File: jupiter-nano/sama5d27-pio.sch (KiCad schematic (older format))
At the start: 3 parts

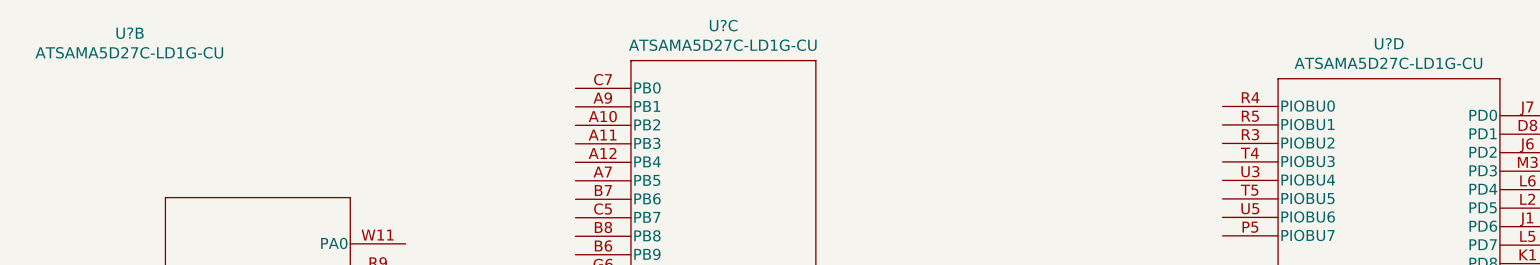
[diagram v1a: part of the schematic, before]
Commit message: WIP some work on clocking
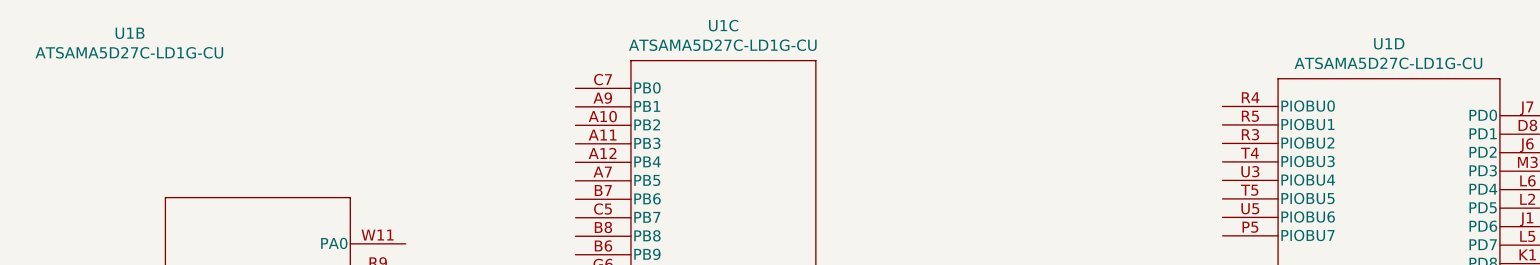
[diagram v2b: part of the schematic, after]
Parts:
- gave numbers to parts that had none: 1
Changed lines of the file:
@@
 $EndDescr
 $Comp
-L ATSAMA5D27C-LD1G:ATSAMA5D27C-LD1G-CU U?
+L ATSAMA5D27C-LD1G:ATSAMA5D27C-LD1G-CU U1
 U 2 1 5F5990A8
 P 2382 1089
-F 0 "U?" H 1740 1576 60  0000 C CNN
+F 0 "U1" H 1740 1576 60  0000 C CNN
 F 1 "ATSAMA5D27C-LD1G-CU" H 1740 1470 60  0000 C CNN
 F 2 "TFBGA361_16X16_MCH" H 3582 1429 60  0001 C CNN
@@
 $EndComp
 $Comp
-L ATSAMA5D27C-LD1G:ATSAMA5D27C-LD1G-CU U?
+L ATSAMA5D27C-LD1G:ATSAMA5D27C-LD1G-CU U1
 U 3 1 5F5A7AFC
 P 4150 948
-F 0 "U?" H 4950 1335 60  0000 C CNN
+F 0 "U1" H 4950 1335 60  0000 C CNN
 F 1 "ATSAMA5D27C-LD1G-CU" H 4950 1229 60  0000 C CNN
 F 2 "TFBGA361_16X16_MCH" H 5350 1288 60  0001 C CNN
@@
 $EndComp
 $Comp
-L ATSAMA5D27C-LD1G:ATSAMA5D27C-LD1G-CU U?
+L ATSAMA5D27C-LD1G:ATSAMA5D27C-LD1G-CU U1
 U 4 1 5F5C0676
 P 7650 1046
-F 0 "U?" H 8550 1433 60  0000 C CNN
+F 0 "U1" H 8550 1433 60  0000 C CNN
 F 1 "ATSAMA5D27C-LD1G-CU" H 8550 1327 60  0000 C CNN
 F 2 "TFBGA361_16X16_MCH" H 8850 1386 60  0001 C CNN

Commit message: WIP, PIO done
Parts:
- added R14: 100K, symbol Device:R_Small
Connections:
- net labels added: AD0, AD1, AD2, AD3, AD4, AD5, ADTRG-IRQ, FLEXCOM4_IO1, GND, I2C_TWCK0, I2C_TWCK1, I2C_TWD0, I2C_TWD1, LOWQ#, PIOBU1, PIOBU2, PIOBU3, PIOBU4, PIOBU5, PIOBU6, PIOBU7, PMIC_CHLEV_PA12, PMIC_IRQ_B13, PMIC_LBO, PWMEXTRAG1-IRQ, PWMH1, PWMH2, PWMH3, PWML0, SDMMC_CD, SDMMC_CK, SDMMC_CMD, SDMMC_DAT0, SDMMC_DAT1, SDMMC_DAT2, SDMMC_DAT3, SPI_MISO, SPI_MOSI, STATUS_LED, TMS, UART1_RX, UART1_TX
- wire segments 0 -> 47
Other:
- moved on the sheet: U1B, U1C, U1D
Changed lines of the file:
@@
 L ATSAMA5D27C-LD1G:ATSAMA5D27C-LD1G-CU U1
 U 2 1 5F5990A8
-P 2382 1089
-F 0 "U1" H 1740 1576 60  0000 C CNN
-F 1 "ATSAMA5D27C-LD1G-CU" H 1740 1470 60  0000 C CNN
-F 2 "TFBGA361_16X16_MCH" H 3582 1429 60  0001 C CNN
-F 3 "" H 2382 1089 60  0000 C CNN
-	2    2382 1089
-	1    0    0    -1
-$EndComp
+P 1150 600
+F 0 "U1" H 1195 400 60  0000 C CNN
+F 1 "ATSAMA5D27C-LD1G-CU" H 1195 300 60  0000 C CNN
+F 2 "TFBGA361_16X16_MCH" H 2350 940 60  0001 C CNN
+F 3 "" H 1150 600 60  0000 C CNN
+	2    1150 600
+	1    0    0    -1
+$EndComp
+$Comp
+L ATSAMA5D27C-LD1G:ATSAMA5D27C-LD1G-CU U1
+U 4 1 5F5C0676
+P 7250 1400
+F 0 "U1" H 8150 1787 60  0000 C CNN
+F 1 "ATSAMA5D27C-LD1G-CU" H 8150 1681 60  0000 C CNN
+F 2 "TFBGA361_16X16_MCH" H 8450 1740 60  0001 C CNN
+F 3 "" H 7250 1400 60  0000 C CNN
+	4    7250 1400
+	1    0    0    -1
+$EndComp
+Wire Wire Line
+	2000 2150 2250 2150
+Text GLabel 2250 2150 2    50   Input ~ 0
+STATUS_LED
+Text GLabel 2250 3050 2    50   Input ~ 0
+PMIC_CHLEV_PA12
+Text GLabel 2250 3500 2    50   Input ~ 0
+SPI_MOSI
+Text GLabel 2250 3650 2    50   Input ~ 0
+SPI_MISO
+Text GLabel 2250 3950 2    50   Input ~ 0
+SDMMC_DAT0
+Text GLabel 2200 4100 2    50   Input ~ 0
+SDMMC_DAT1
+Text GLabel 2200 4250 2    50   Input ~ 0
+SDMMC_DAT2
+Text GLabel 2250 4400 2    50   Input ~ 0
+SDMMC_DAT3
+Text GLabel 2250 4550 2    50   Input ~ 0
+SDMMC_CK
+Text GLabel 2250 5450 2    50   Input ~ 0
+SDMMC_CMD
+Text GLabel 2250 5750 2    50   Input ~ 0
+SDMMC_CD
+Text GLabel 2250 5900 2    50   Input ~ 0
+PWML0
+Text GLabel 3900 1500 0    50   Input ~ 0
+PWML0
+Wire Wire Line
+	2000 3050 2250 3050
+Wire Wire Line
+	2000 3500 2250 3500
+Wire Wire Line
+	2000 3650 2250 3650
 $Comp
 L ATSAMA5D27C-LD1G:ATSAMA5D27C-LD1G-CU U1
 U 3 1 5F5A7AFC
-P 4150 948
-F 0 "U1" H 4950 1335 60  0000 C CNN
-F 1 "ATSAMA5D27C-LD1G-CU" H 4950 1229 60  0000 C CNN
-F 2 "TFBGA361_16X16_MCH" H 5350 1288 60  0001 C CNN
-F 3 "" H 4150 948 60  0000 C CNN
-	3    4150 948
-	1    0    0    -1
-$EndComp
-$Comp
-L ATSAMA5D27C-LD1G:ATSAMA5D27C-LD1G-CU U1
-U 4 1 5F5C0676
-P 7650 1046
-F 0 "U1" H 8550 1433 60  0000 C CNN
-F 1 "ATSAMA5D27C-LD1G-CU" H 8550 1327 60  0000 C CNN
-F 2 "TFBGA361_16X16_MCH" H 8850 1386 60  0001 C CNN
-F 3 "" H 7650 1046 60  0000 C CNN
-	4    7650 1046
-	1    0    0    -1
+P 4150 1450
+F 0 "U1" H 4950 1837 60  0000 C CNN
+F 1 "ATSAMA5D27C-LD1G-CU" H 4950 1731 60  0000 C CNN
+F 2 "TFBGA361_16X16_MCH" H 5350 1790 60  0001 C CNN
+F 3 "" H 4150 1450 60  0000 C CNN
+	3    4150 1450
+	1    0    0    -1
+$EndComp
+Wire Wire Line
+	2000 1250 2100 1250
+Wire Wire Line
+	2000 1400 2100 1400
+Wire Wire Line
+	4150 1400 3900 1400
+Wire Wire Line
+	3900 1500 4150 1500
+Wire Wire Line
+	2000 3950 2250 3950
+Wire Wire Line
+	2000 4100 2200 4100
+Wire Wire Line
+	2000 4250 2200 4250
+Wire Wire Line
+	2000 4400 2250 4400
+Wire Wire Line
+	2000 4550 2250 4550
+Wire Wire Line
+	2000 5450 2250 5450
+Wire Wire Line
+	2000 5750 2250 5750
+Wire Wire Line
+	2000 5900 2250 5900
+Text GLabel 3900 1400 0    50   Input ~ 0
+PWMH1
+Text GLabel 3900 1700 0    50   Input ~ 0
+PWMEXTRAG1-IRQ
+Text GLabel 3900 1900 0    50   Input ~ 0
+PWMH2
+Text GLabel 3900 2100 0    50   Input ~ 0
+PWMH3
+Wire Wire Line
+	3900 1700 4150 1700
+Wire Wire Line
+	3900 1900 4150 1900
+Wire Wire Line
+	3900 2100 4150 2100
+Text GLabel 3900 2700 0    50   Input ~ 0
+PMIC_IRQ_B13
+Text GLabel 3950 4500 0    50   Input ~ 0
+I2C_TWD0
+Wire Wire Line
+	3950 4500 4150 4500
+Wire Wire Line
+	3900 2700 4150 2700
+Wire Wire Line
+	5750 2650 6000 2650
+Text GLabel 6000 2650 2    50   Input ~ 0
+I2C_TWCK0
+Wire Wire Line
+	5750 3450 6000 3450
+Text GLabel 6000 3450 2    50   Input ~ 0
+PMIC_LBO
+Wire Wire Line
+	7250 1350 7050 1350
+Wire Wire Line
+	7250 1450 7050 1450
+Wire Wire Line
+	7250 1550 7050 1550
+Wire Wire Line
+	7250 1650 7050 1650
+Wire Wire Line
+	7250 1750 7050 1750
+Wire Wire Line
+	7250 1850 7050 1850
+Wire Wire Line
+	7250 1950 7050 1950
+Wire Wire Line
+	7250 2050 7050 2050
+Text GLabel 7050 1350 0    50   Input ~ 0
+LOWQ#
+Text GLabel 7050 1450 0    50   Input ~ 0
+PIOBU1
+Text GLabel 7050 1550 0    50   Input ~ 0
+PIOBU2
+Text GLabel 7050 1650 0    50   Input ~ 0
+PIOBU3
+Text GLabel 7050 1750 0    50   Input ~ 0
+PIOBU4
+Text GLabel 7050 1850 0    50   Input ~ 0
+PIOBU5
+Text GLabel 7050 1950 0    50   Input ~ 0
+PIOBU6
+Text GLabel 7050 2050 0    50   Input ~ 0
+PIOBU7
+Wire Wire Line
+	9050 1600 9100 1600
+Text GLabel 9200 1600 2    50   Input ~ 0
+UART1_RX
+Wire Wire Line
+	9050 1700 9200 1700
+Text GLabel 9200 1700 2    50   Input ~ 0
+UART1_TX
+Wire Wire Line
+	9050 1800 9200 1800
+Wire Wire Line
+	9050 1900 9200 1900
+Text GLabel 9200 1800 2    50   Input ~ 0
+I2C_TWD1
+Text GLabel 9200 1900 2    50   Input ~ 0
+I2C_TWCK1
+Wire Wire Line
+	9050 2700 9200 2700
+Wire Wire Line
+	9050 3100 9200 3100
+Wire Wire Line
+	9050 3300 9200 3300
+Wire Wire Line
+	9050 3400 9200 3400
+Wire Wire Line
+	9050 3500 9200 3500
+Wire Wire Line
+	9050 3600 9200 3600
+Wire Wire Line
+	9050 3700 9200 3700
+Wire Wire Line
+	9050 3800 9200 3800
+Text GLabel 9200 2700 2    50   Input ~ 0
+FLEXCOM4_IO1
+Text GLabel 9200 3100 2    50   Input ~ 0
+TMS
+Text GLabel 9200 3300 2    50   Input ~ 0
+AD0
+Text GLabel 9200 3400 2    50   Input ~ 0
+AD1
+Text GLabel 9200 3500 2    50   Input ~ 0
+AD2
+Text GLabel 9200 3600 2    50   Input ~ 0
+AD3
+Text GLabel 9200 3700 2    50   Input ~ 0
+AD4
+Text GLabel 9200 3800 2    50   Input ~ 0
+AD5
+Wire Wire Line
+	9050 4500 9200 4500
+Text GLabel 9200 4500 2    50   Input ~ 0
+ADTRG-IRQ
+$Comp
+L Device:R_Small R14
+U 1 1 600D6DFE
+P 9100 1050
+F 0 "R14" H 9159 1096 50  0000 L CNN
+F 1 "100K" H 9159 1005 50  0000 L CNN
+F 2 "" H 9100 1050 50  0001 C CNN
+F 3 "~" H 9100 1050 50  0001 C CNN
+	1    9100 1050
+	1    0    0    -1
+$EndComp
+Wire Wire Line
+	9100 1150 9100 1600
+Connection ~ 9100 1600
+Wire Wire Line
+	9100 1600 9200 1600
+Wire Wire Line
+	9100 950  9100 850
+$Comp
+L power:GND #PWR?
+U 1 1 600DB627
+P 9100 850
+F 0 "#PWR?" H 9100 600 50  0001 C CNN
+F 1 "GND" H 9105 677 50  0000 C CNN
+F 2 "" H 9100 850 50  0001 C CNN
+F 3 "" H 9100 850 50  0001 C CNN
+	1    9100 850
+	-1   0    0    1
 $EndComp
 $EndSCHEMATC

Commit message: WIP, USB-UART and JTAG done
- minor clean up and SD Card form factor still left
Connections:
- net labels added: JTAG_TCK_PD14, JTAG_TDI_PD15, JTAG_TDO_PD16, JTAG_TMS_PD17
- net labels removed: TMS
- wire segments 47 -> 50
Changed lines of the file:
@@
 FLEXCOM4_IO1
 Text GLabel 9200 3100 2    50   Input ~ 0
-TMS
+JTAG_TMS_PD17
 Text GLabel 9200 3300 2    50   Input ~ 0
 AD0
@@
 	-1   0    0    1
 $EndComp
+Wire Wire Line
+	9050 2800 9200 2800
+Wire Wire Line
+	9050 3000 9200 3000
+Wire Wire Line
+	9050 2900 9200 2900
+Text GLabel 9200 3000 2    50   Input ~ 0
+JTAG_TDO_PD16
+Text GLabel 9200 2900 2    50   Input ~ 0
+JTAG_TDI_PD15
+Text GLabel 9200 2800 2    50   Input ~ 0
+JTAG_TCK_PD14
 $EndSCHEMATC

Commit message: cleanup
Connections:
- net labels added: SDMMC_CARD_DET
- wire segments 50 -> 51
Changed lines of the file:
@@
 Text GLabel 9200 2800 2    50   Input ~ 0
 JTAG_TCK_PD14
+Text GLabel 2250 5600 2    50   Input ~ 0
+SDMMC_CARD_DET
+Wire Wire Line
+	2000 5600 2250 5600
 $EndSCHEMATC

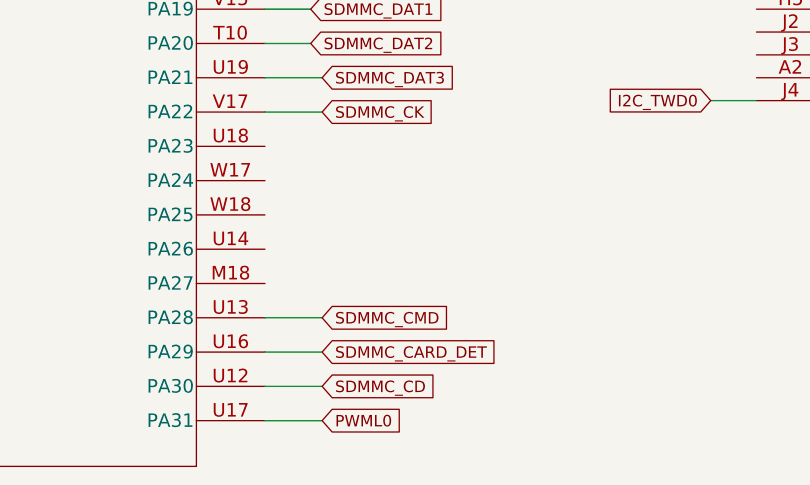
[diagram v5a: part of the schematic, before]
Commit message: add USBA VBUS sense; remove mounting holes
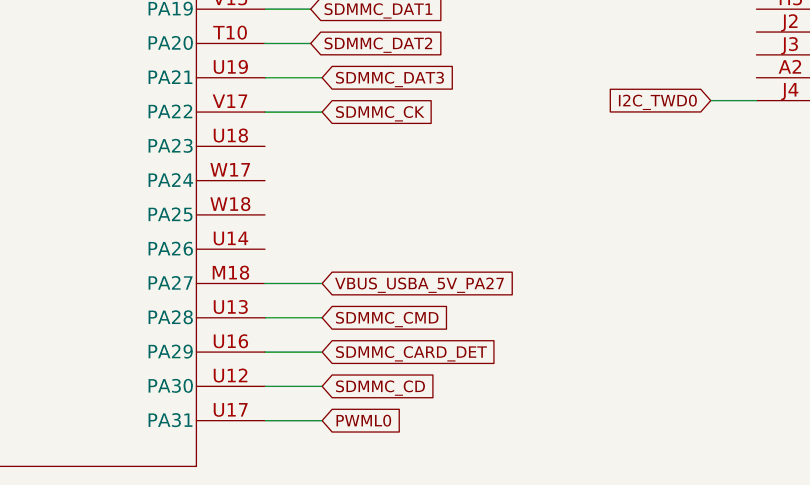
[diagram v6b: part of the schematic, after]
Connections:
- net VBUS_USBA_5V_PA27: now reaches U1.M18 (PA27)
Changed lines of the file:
@@
 Wire Wire Line
 	2000 5600 2250 5600
+Wire Wire Line
+	2000 5300 2250 5300
+Text GLabel 2250 5300 2    50   Input ~ 0
+VBUS_USBA_5V_PA27
 $EndSCHEMATC
